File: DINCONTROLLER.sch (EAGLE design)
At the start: 44 parts, among them IC1 ESPWROOM32, SW1 TAC-SWITCH-LEDSP0620, SW2 TAC-SWITCH-LEDSP0620, SW3 TAC-SWITCH-LEDSP0620, SW4 TAC-SWITCH-LEDSP0620, SW5 TAC-SWITCH-LEDSP0620, SW6 TAC-SWITCH-LEDSP0620, SW7 TAC-SWITCH-LEDSP0620, SW8 TAC-SWITCH-LEDSP0620

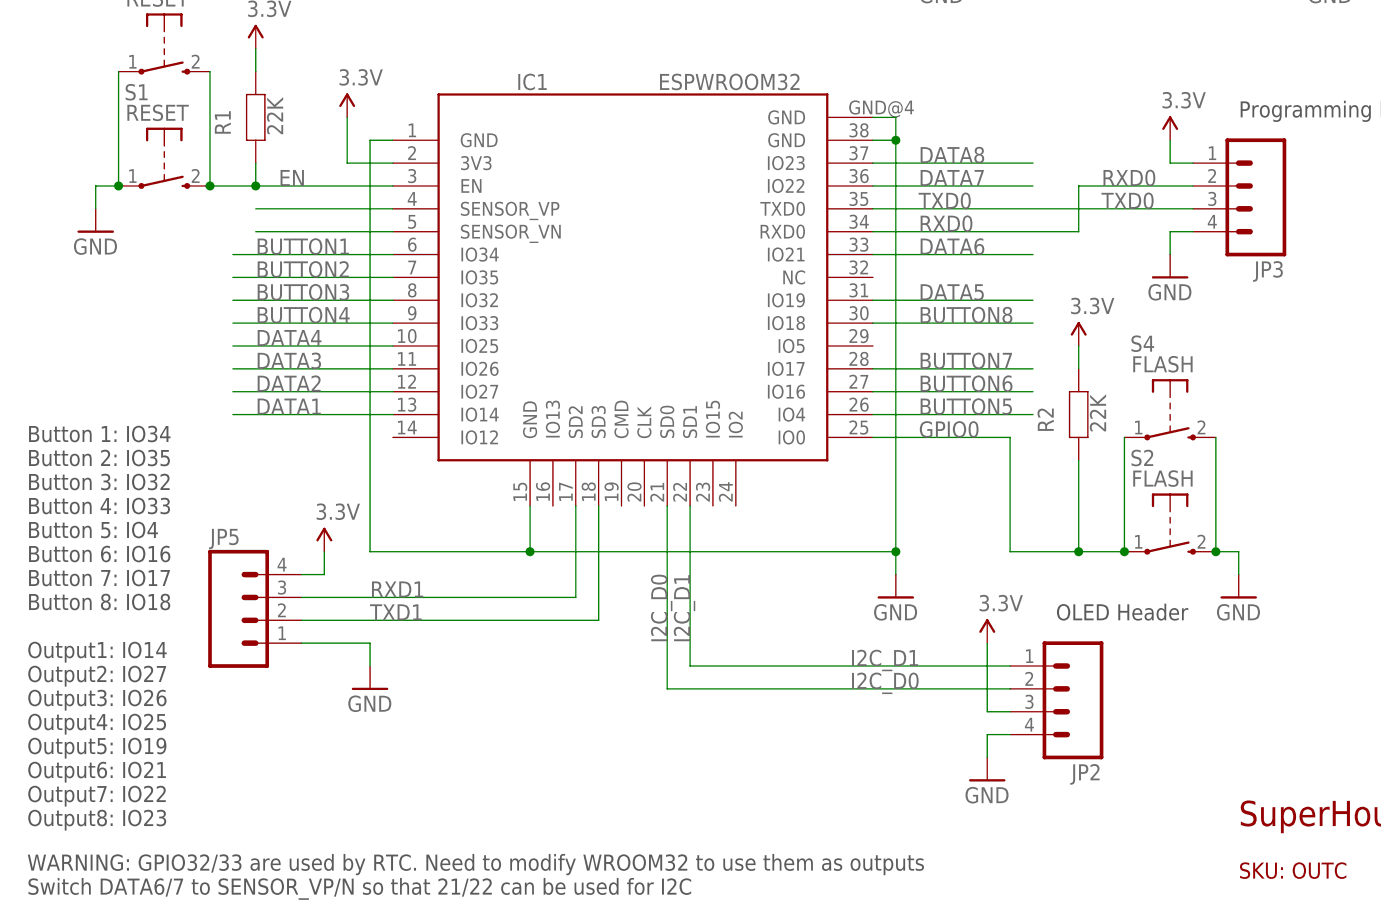
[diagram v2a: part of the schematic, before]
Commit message: Major update: remapped IO pins for v1.1 release
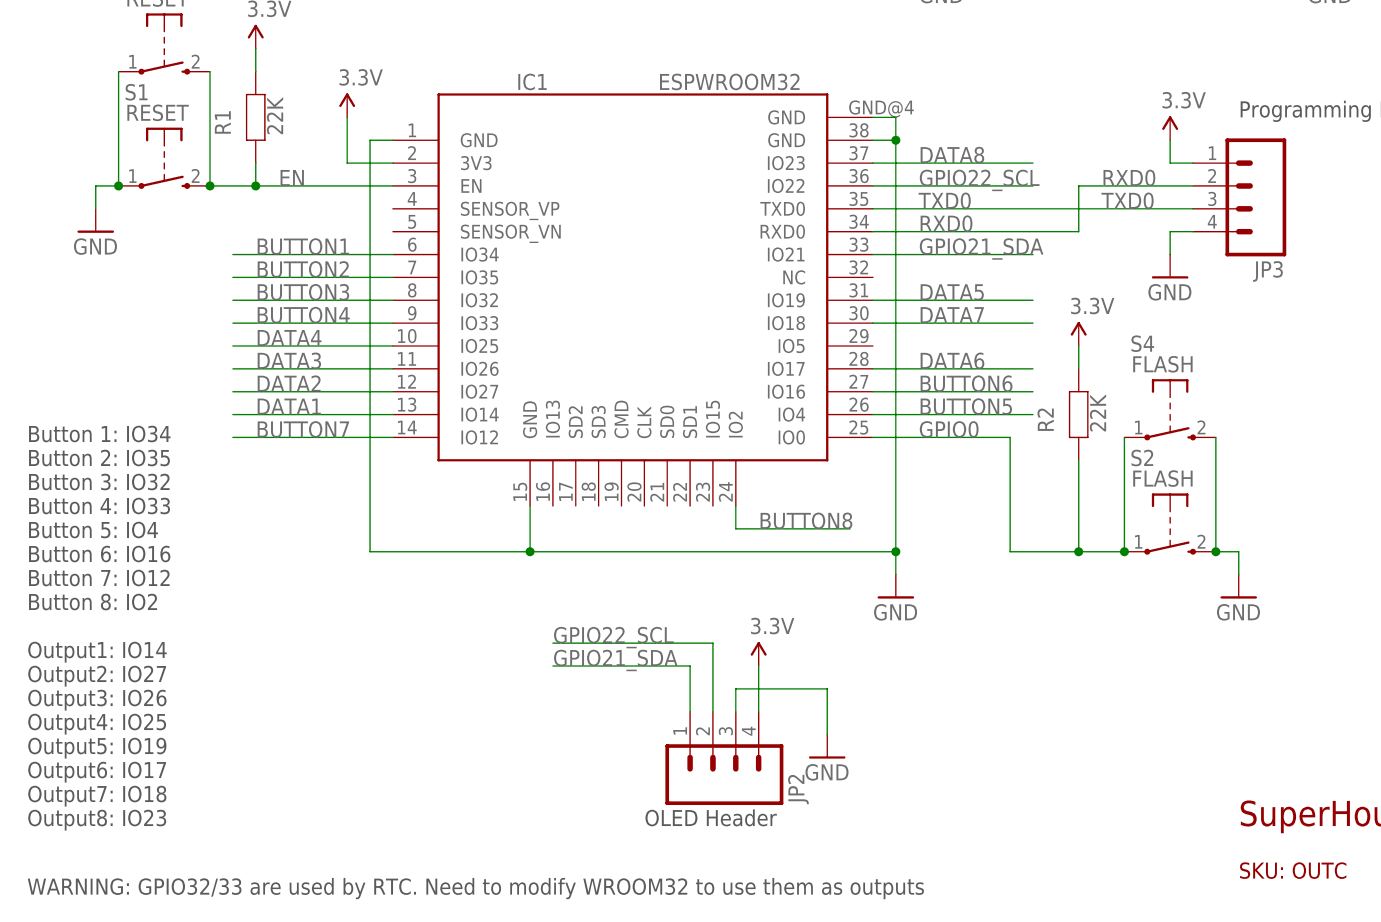
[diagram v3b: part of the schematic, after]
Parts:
- removed JP5: (no value), freetronics-jon:M04PTH
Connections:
- removed net I2C_D0: IC1.SD0, JP2.2
- removed net I2C_D1: IC1.SD1, JP2.1
- removed net N$20: IC1.SENSOR_VP
- removed net N$21: IC1.SENSOR_VN
- removed net RXD1: IC1.SD2, JP5.3
- removed net TXD1: IC1.SD3, JP5.2
- new net GPIO21_SDA: IC1.IO21, JP2.1
- new net GPIO22_SCL: IC1.IO22, JP2.2
- net 3.3V: now also JP2.4; no longer JP2.3, JP5.4
- net BUTTON7: now also IC1.IO12; no longer IC1.IO17
- net BUTTON8: now also IC1.IO2; no longer IC1.IO18
- net DATA6: now also IC1.IO17; no longer IC1.IO21
- net DATA7: now also IC1.IO18; no longer IC1.IO22
- net GND: now also JP2.3; no longer JP2.4, JP5.1
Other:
- note added: "Button 1: IO34 Button 2: IO35 Button 3: IO32 Button 4: IO33 Button 5: IO4 Button 6: IO16 Button 7: IO12 Button 8: IO2 Output1: IO14 Output2: IO27 Output3: IO26 Output4: IO25 Output5: IO19 Output6: IO17 Output7: IO18 Output8: IO23"
- note added: "WARNING: GPIO32/33 are used by RTC. Need to modify WROOM32 to use them as outputs"
- note removed: "Button 1: IO34 Button 2: IO35 Button 3: IO32 Button 4: IO33 Button 5: IO4 Button 6: IO16 Button 7: IO17 Button 8: IO18 Output1: IO14 Output2: IO27 Output3: IO26 Output4: IO25 Output5: IO19 Output6: IO21 Output7: IO22 Output8: IO23"
- note removed: "WARNING: GPIO32/33 are used by RTC. Need to modify WROOM32 to use them as outputs Switch DATA6/7 to SENSOR_VP/N so that 21/22 can be used for I2C"
- moved on the sheet: JP2
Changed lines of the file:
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@@
 <part name="R2" library="freetronics" deviceset="RESISTOR" device="0603" value="22K"/>
 <part name="P+9" library="freetronics-original" deviceset="3.3V" device=""/>
-<part name="GND10" library="SparkFun" deviceset="GND" device=""/>
 <part name="IC1" library="freetronics-jon" deviceset="ESPWROOM32" device=""/>
 <part name="R3" library="freetronics" deviceset="RESISTOR" device="0603" value="22K"/>
@@
 <part name="S3" library="freetronics-jon" deviceset="TAC_SWITCH_2PIN" device="SMT" value="RESET"/>
 <part name="S4" library="freetronics-jon" deviceset="TAC_SWITCH_2PIN" device="SMT" value="FLASH"/>
-<part name="JP5" library="freetronics-jon" deviceset="M04" device="PTH"/>
-<part name="P+18" library="freetronics-original" deviceset="3.3V" device=""/>
 </parts>
 <sheets>
@@
 Button 5: IO4
 Button 6: IO16
-Button 7: IO17
-Button 8: IO18
+Button 7: IO12
+Button 8: IO2
 Output1: IO14
 Output2: IO27
@@
 Output4: IO25
 Output5: IO19
-Output6: IO21
-Output7: IO22
+Output6: IO17
+Output7: IO18
 Output8: IO23</text>
 <text x="7.62" y="132.08" size="1.778" layer="97">VCC is VIN from main board
@@
 <text x="170.18" y="86.36" size="1.778" layer="94">800mA</text>
 <text x="12.7" y="142.24" size="1.778" layer="97">(IOREF)</text>
-<text x="7.62" y="5.08" size="1.778" layer="97">WARNING: GPIO32/33 are used by RTC. Need to modify WROOM32 to use them as outputs
-Switch DATA6/7 to SENSOR_VP/N so that 21/22 can be used for I2C</text>
-<text x="121.92" y="35.56" size="1.778" layer="97">OLED Header</text>
+<text x="7.62" y="5.08" size="1.778" layer="97">WARNING: GPIO32/33 are used by RTC. Need to modify WROOM32 to use them as outputs</text>
+<text x="76.2" y="12.7" size="1.778" layer="97">OLED Header</text>
 <text x="142.24" y="91.44" size="1.778" layer="97">Programming Header</text>
 <text x="53.34" y="144.78" size="1.778" layer="97">(RESET)</text>
@@
 <instance part="P+2" gate="G$1" x="43.18" y="91.44"/>
 <instance part="LED10" gate="G$1" x="223.52" y="71.12"/>
-<instance part="JP2" gate="G$1" x="121.92" y="27.94" rot="R180"/>
-<instance part="GND2" gate="1" x="114.3" y="17.78"/>
-<instance part="P+3" gate="G$1" x="114.3" y="33.02"/>
+<instance part="JP2" gate="G$1" x="83.82" y="20.32" rot="MR90"/>
+<instance part="GND2" gate="1" x="96.52" y="20.32"/>
+<instance part="P+3" gate="G$1" x="88.9" y="30.48"/>
 <instance part="P+4" gate="1" x="10.16" y="160.02"/>
 <instance part="P+5" gate="1" x="170.18" y="78.74"/>
@@
 </instance>
 <instance part="P+9" gate="G$1" x="124.46" y="66.04"/>
-<instance part="GND10" gate="1" x="45.72" y="27.94"/>
 <instance part="IC1" gate="IC$1" x="73.66" y="73.66"/>
 <instance part="R3" gate="G$1" x="81.28" y="167.64" smashed="yes" rot="R270">
@@
 <instance part="S3" gate="1" x="22.86" y="96.52"/>
 <instance part="S4" gate="1" x="134.62" y="55.88"/>
-<instance part="JP5" gate="G$1" x="33.02" y="35.56"/>
-<instance part="P+18" gate="G$1" x="40.64" y="43.18"/>
 </instances>
 <busses>
@@
 </segment>
 <segment>
-<wire x1="38.1" y1="33.02" x2="45.72" y2="33.02" width="0.1524" layer="91"/>
-<pinref part="GND10" gate="1" pin="GND"/>
-<wire x1="45.72" y1="33.02" x2="45.72" y2="30.48" width="0.1524" layer="91"/>
-<pinref part="JP5" gate="G$1" pin="1"/>
-</segment>
-<segment>
+<pinref part="JP2" gate="G$1" pin="3"/>
+<wire x1="86.36" y1="25.4" x2="86.36" y2="27.94" width="0.1524" layer="91"/>
+<wire x1="86.36" y1="27.94" x2="96.52" y2="27.94" width="0.1524" layer="91"/>
 <pinref part="GND2" gate="1" pin="GND"/>
-<wire x1="114.3" y1="20.32" x2="114.3" y2="22.86" width="0.1524" layer="91"/>
-<pinref part="JP2" gate="G$1" pin="4"/>
-<wire x1="114.3" y1="22.86" x2="116.84" y2="22.86" width="0.1524" layer="91"/>
+<wire x1="96.52" y1="27.94" x2="96.52" y2="22.86" width="0.1524" layer="91"/>
 </segment>
 </net>
@@
 </segment>
 <segment>
-<wire x1="101.6" y1="83.82" x2="119.38" y2="83.82" width="0.1524" layer="91"/>
-<label x="106.68" y="83.82" size="1.778" layer="95"/>
-<pinref part="IC1" gate="IC$1" pin="IO22"/>
+<wire x1="101.6" y1="68.58" x2="119.38" y2="68.58" width="0.1524" layer="91"/>
+<label x="106.68" y="68.58" size="1.778" layer="95"/>
+<pinref part="IC1" gate="IC$1" pin="IO18"/>
 </segment>
 </net>
@@
 </segment>
 <segment>
-<wire x1="119.38" y1="76.2" x2="101.6" y2="76.2" width="0.1524" layer="91"/>
-<label x="106.68" y="76.2" size="1.778" layer="95"/>
-<pinref part="IC1" gate="IC$1" pin="IO21"/>
+<wire x1="101.6" y1="63.5" x2="119.38" y2="63.5" width="0.1524" layer="91"/>
+<label x="106.68" y="63.5" size="1.778" layer="95"/>
+<pinref part="IC1" gate="IC$1" pin="IO17"/>
 </segment>
 </net>
@@
 </segment>
 <segment>
-<pinref part="P+3" gate="G$1" pin="3.3V"/>
-<wire x1="114.3" y1="33.02" x2="114.3" y2="25.4" width="0.1524" layer="91"/>
-<pinref part="JP2" gate="G$1" pin="3"/>
-<wire x1="114.3" y1="25.4" x2="116.84" y2="25.4" width="0.1524" layer="91"/>
-</segment>
-<segment>
 <pinref part="R3" gate="G$1" pin="1"/>
 <pinref part="P+10" gate="G$1" pin="3.3V"/>
@@
 </segment>
 <segment>
-<pinref part="JP5" gate="G$1" pin="4"/>
-<wire x1="38.1" y1="40.64" x2="40.64" y2="40.64" width="0.1524" layer="91"/>
-<pinref part="P+18" gate="G$1" pin="3.3V"/>
-<wire x1="40.64" y1="40.64" x2="40.64" y2="43.18" width="0.1524" layer="91"/>
-</segment>
-</net>
-<net name="N$20" class="0">
-<segment>
-<wire x1="48.26" y1="81.28" x2="33.02" y2="81.28" width="0.1524" layer="91"/>
-<pinref part="IC1" gate="IC$1" pin="SENSOR_VP"/>
-</segment>
-</net>
-<net name="N$21" class="0">
-<segment>
-<wire x1="48.26" y1="78.74" x2="33.02" y2="78.74" width="0.1524" layer="91"/>
-<pinref part="IC1" gate="IC$1" pin="SENSOR_VN"/>
-</segment>
-</net>
-<net name="I2C_D1" class="0">
-<segment>
-<label x="99.06" y="30.48" size="1.778" layer="95"/>
-<wire x1="81.28" y1="48.26" x2="81.28" y2="30.48" width="0.1524" layer="91"/>
-<label x="81.28" y="33.02" size="1.778" layer="95" rot="R90"/>
-<pinref part="IC1" gate="IC$1" pin="SD1"/>
-<pinref part="JP2" gate="G$1" pin="1"/>
-<wire x1="81.28" y1="30.48" x2="116.84" y2="30.48" width="0.1524" layer="91"/>
-</segment>
-</net>
-<net name="I2C_D0" class="0">
-<segment>
-<wire x1="78.74" y1="48.26" x2="78.74" y2="27.94" width="0.1524" layer="91"/>
-<label x="78.74" y="33.02" size="1.778" layer="95" rot="R90"/>
-<label x="99.06" y="27.94" size="1.778" layer="95"/>
-<pinref part="IC1" gate="IC$1" pin="SD0"/>
-<pinref part="JP2" gate="G$1" pin="2"/>
-<wire x1="78.74" y1="27.94" x2="116.84" y2="27.94" width="0.1524" layer="91"/>
+<pinref part="P+3" gate="G$1" pin="3.3V"/>
+<pinref part="JP2" gate="G$1" pin="4"/>
+<wire x1="88.9" y1="30.48" x2="88.9" y2="25.4" width="0.1524" layer="91"/>
 </segment>
 </net>
@@
 </segment>
 <segment>
-<wire x1="101.6" y1="63.5" x2="119.38" y2="63.5" width="0.1524" layer="91"/>
-<label x="106.68" y="63.5" size="1.778" layer="95"/>
-<pinref part="IC1" gate="IC$1" pin="IO17"/>
+<pinref part="IC1" gate="IC$1" pin="IO12"/>
+<wire x1="48.26" y1="55.88" x2="30.48" y2="55.88" width="0.1524" layer="91"/>
+<label x="33.02" y="55.88" size="1.778" layer="95"/>
 </segment>
 </net>
@@
 </segment>
 <segment>
-<wire x1="101.6" y1="68.58" x2="119.38" y2="68.58" width="0.1524" layer="91"/>
-<label x="106.68" y="68.58" size="1.778" layer="95"/>
-<pinref part="IC1" gate="IC$1" pin="IO18"/>
+<pinref part="IC1" gate="IC$1" pin="IO2"/>
+<wire x1="86.36" y1="48.26" x2="86.36" y2="45.72" width="0.1524" layer="91"/>
+<wire x1="86.36" y1="45.72" x2="99.06" y2="45.72" width="0.1524" layer="91"/>
+<label x="88.9" y="45.72" size="1.778" layer="95"/>
 </segment>
 </net>
@@
 <label x="127" y="83.82" size="1.778" layer="95"/>
 <pinref part="IC1" gate="IC$1" pin="RXD0"/>
-</segment>
-</net>
-<net name="RXD1" class="0">
-<segment>
-<wire x1="68.58" y1="48.26" x2="68.58" y2="38.1" width="0.1524" layer="91"/>
-<wire x1="68.58" y1="38.1" x2="38.1" y2="38.1" width="0.1524" layer="91"/>
-<label x="45.72" y="38.1" size="1.778" layer="95"/>
-<pinref part="IC1" gate="IC$1" pin="SD2"/>
-<pinref part="JP5" gate="G$1" pin="3"/>
-</segment>
-</net>
-<net name="TXD1" class="0">
-<segment>
-<wire x1="71.12" y1="48.26" x2="71.12" y2="35.56" width="0.1524" layer="91"/>
-<wire x1="71.12" y1="35.56" x2="38.1" y2="35.56" width="0.1524" layer="91"/>
-<label x="45.72" y="35.56" size="1.778" layer="95"/>
-<pinref part="IC1" gate="IC$1" pin="SD3"/>
-<pinref part="JP5" gate="G$1" pin="2"/>
 </segment>
 </net>
@@
 </segment>
 </net>
+<net name="GPIO21_SDA" class="0">
+<segment>
+<wire x1="119.38" y1="76.2" x2="101.6" y2="76.2" width="0.1524" layer="91"/>
+<label x="106.68" y="76.2" size="1.778" layer="95"/>
+<pinref part="IC1" gate="IC$1" pin="IO21"/>
+</segment>
+<segment>
+<pinref part="JP2" gate="G$1" pin="1"/>
+<wire x1="81.28" y1="25.4" x2="81.28" y2="30.48" width="0.1524" layer="91"/>
+<wire x1="81.28" y1="30.48" x2="66.04" y2="30.48" width="0.1524" layer="91"/>
+<label x="66.04" y="30.48" size="1.778" layer="95"/>
+</segment>
+</net>
+<net name="GPIO22_SCL" class="0">
+<segment>
+<wire x1="101.6" y1="83.82" x2="119.38" y2="83.82" width="0.1524" layer="91"/>
+<label x="106.68" y="83.82" size="1.778" layer="95"/>
+<pinref part="IC1" gate="IC$1" pin="IO22"/>
+</segment>
+<segment>
+<pinref part="JP2" gate="G$1" pin="2"/>
+<wire x1="83.82" y1="25.4" x2="83.82" y2="33.02" width="0.1524" layer="91"/>
+<wire x1="83.82" y1="33.02" x2="66.04" y2="33.02" width="0.1524" layer="91"/>
+<label x="66.04" y="33.02" size="1.778" layer="95"/>
+</segment>
+</net>
